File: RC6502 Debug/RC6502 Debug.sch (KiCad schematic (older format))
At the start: 19 parts, among them J1 RC6502_Backplane, SW1 STEP, SW2 SI/SC, SW3 RUN, SW4 LE_SEL, U1 MC14495P1, U2 74LS74, U3 MC14495P1, U4 MC14495P1, U5 MC14495P1, U6 MC14495P1, U7 MC14495P1

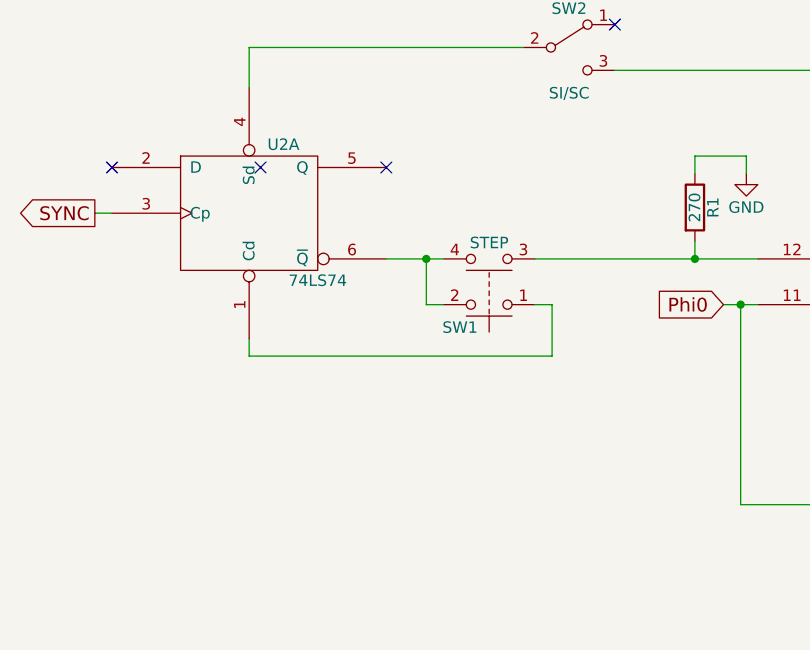
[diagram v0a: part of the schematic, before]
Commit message: Exported schematic to pdf
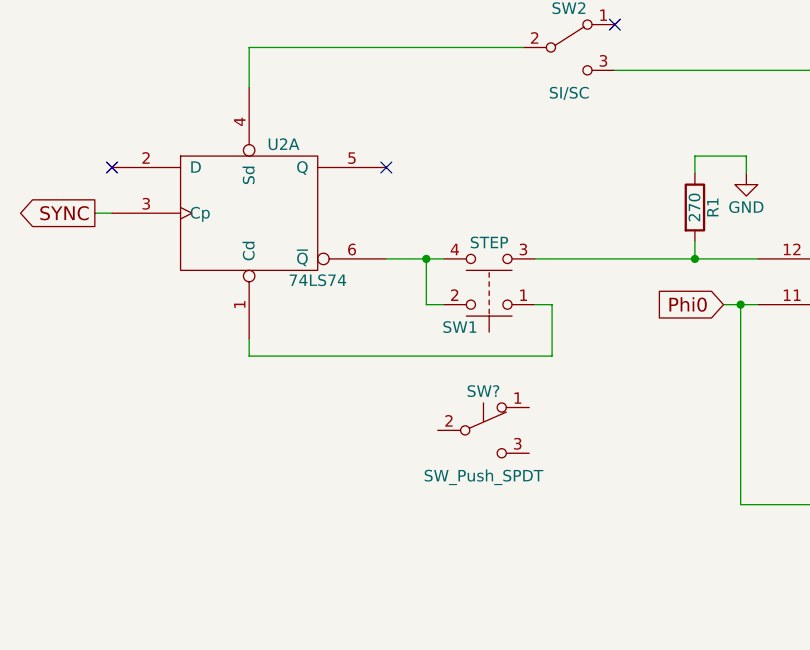
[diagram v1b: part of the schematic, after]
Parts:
- added SW?: SW_Push_SPDT, symbol SW_Push_SPDT
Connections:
- no-connect marks 30 -> 29
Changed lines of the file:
@@
 Text GLabel 2775 6475 0    60   Output ~ 0
 SYNC
-NoConn ~ 3500 6275
 NoConn ~ 6275 7425
 Text GLabel 5525 6875 0    60   Input ~ 0
@@
 Text Notes 11875 10300 0    60   ~ 0
 RC6502 Debug card, adding bus monitor features and a single step circuit to the\ncomputer in order to aid with software and hardware development. Based on schematic\nincluded in the original Apple 1 manual.
+$Comp
+L SW_Push_SPDT SW?
+U 1 1 5C205A95
+P 4475 7425
+F 0 "SW?" H 4475 7595 50  0000 C CNN
+F 1 "SW_Push_SPDT" H 4475 7225 50  0000 C CNN
+F 2 "" H 4475 7425 50  0001 C CNN
+F 3 "" H 4475 7425 50  0001 C CNN
+	1    4475 7425
+	1    0    0    -1
+$EndComp
 $EndSCHEMATC

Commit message: Debug module schematic reworked
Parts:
- removed SW?: SW_Push_SPDT, symbol SW_Push_SPDT
- added C1: CP, symbol CP
- added D1, D2, D3, D4, D5, D6, D7, D8: (no value), symbol LED_Small
- added R2, R3, R4, R5, R6, R7, R8, R9: 220, symbol R
- added U8: 74LS04, symbol 74LS04
- added U9: 74LS374, symbol 74LS374
- renumbered SW4 to SW6, U2 to U1, U1 to U2
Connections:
- net GND: now also R1.2, C1.2, D1.1 (K), D2.1 (K), D3.1 (K), D4.1 (K), D5.1 (K), D6.1 (K), D7.1 (K), D8.1 (K), U8.11, U8.13, U8.3, U8.5, U8.7 (GND), U8.7 (GND), U8.7 (GND), U8.7 (GND), U8.7 (GND), U8.7 (GND), U8.9, U9.1 (OE), U9.10 (GND); no longer R1.1
- net RDY: now also U9.3 (D0)
- net SYNC: now also U9.4 (D1)
- net VCC: now also C1.1, U8.14 (VCC), U8.14 (VCC), U8.14 (VCC), U8.14 (VCC), U8.14 (VCC), U8.14 (VCC), U9.20 (VCC)
- net ~LE: now also U8.2, U9.11 (Cp); no longer SW6.2 (B)
- net Phi2: now reaches J1.19 (PHI2)
- net Phi2: now also U9.18 (D7)
- net RESET: now reaches J1.20 (RESET)
- net RESET: now also U9.8 (D3)
- net IRQ: now reaches J1.22 (IRQ)
- net IRQ: now also U9.13 (D4)
- net Phi1: now reaches J1.23 (PHI1)
- net Phi1: now also SW6.1 (A), U1.11 (Cp), U9.17 (D6)
- net RW: now reaches J1.24 (RW)
- net RW: now also U9.7 (D2)
- net NMI: now reaches J1.37 (NMI)
- net NMI: now also U9.14 (D5)
- net at SW1.3, U1.12 (D): now also R1.1; no longer R1.2
- net Step: now reaches SW2.3 (C), SW6.3 (C), U1.8 (~Q)
- removed net Phi0: J1.21 (PHI0), SW6.1 (A), U1.11 (Cp)
- new net: SW6.2 (B), U8.1
- new net: R6.1, U9.12 (O4)
- new net: R7.1, U9.15 (O5)
- new net: R8.1, U9.16 (O6)
- new net: R9.1, U9.19 (O7)
- new net: R2.1, U9.2 (O0)
- new net: R3.1, U9.5 (O1)
- new net: R4.1, U9.6 (O2)
- new net: R5.1, U9.9 (O3)
- new net: D1.2 (A), R2.2
- new net: D2.2 (A), R3.2
- new net: D3.2 (A), R4.2
- new net: D4.2 (A), R5.2
- new net: D5.2 (A), R6.2
- new net: D6.2 (A), R7.2
- new net: D7.2 (A), R8.2
- new net: D8.2 (A), R9.2
- no-connect marks 29 -> 30
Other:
- moved on the sheet: AFF1, AFF2, AFF3, AFF4, AFF5, AFF6, R1, SW1, SW2, SW3, SW6, U1A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
